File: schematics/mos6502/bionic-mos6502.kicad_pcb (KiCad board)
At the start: 2 copper layers, 48.3 x 71.1 mm, 10 parts, among them J1 Bionic-P135, J2 Bionic-P245, U1 W65C816S, U2 74HC126, U3 11AA010-I/TO

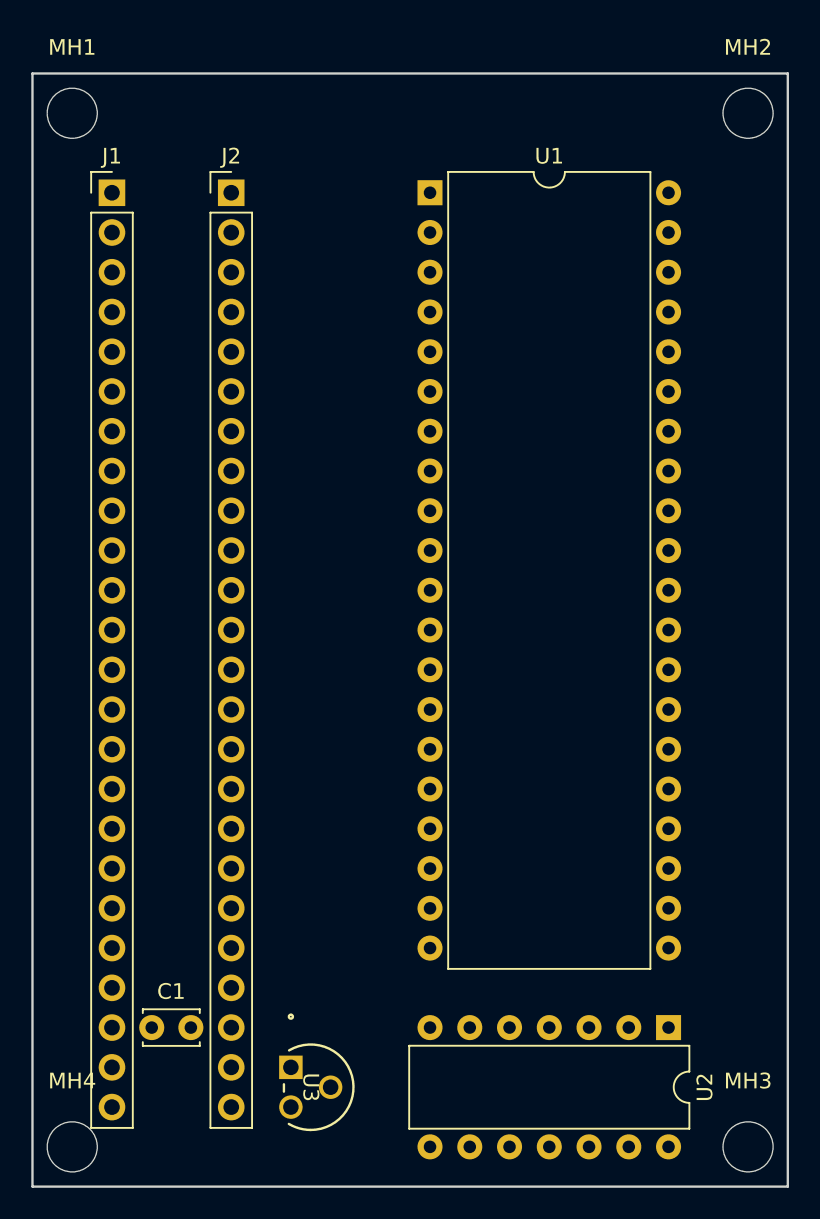
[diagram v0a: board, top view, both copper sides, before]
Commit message: [MOS6502] Remove HC126
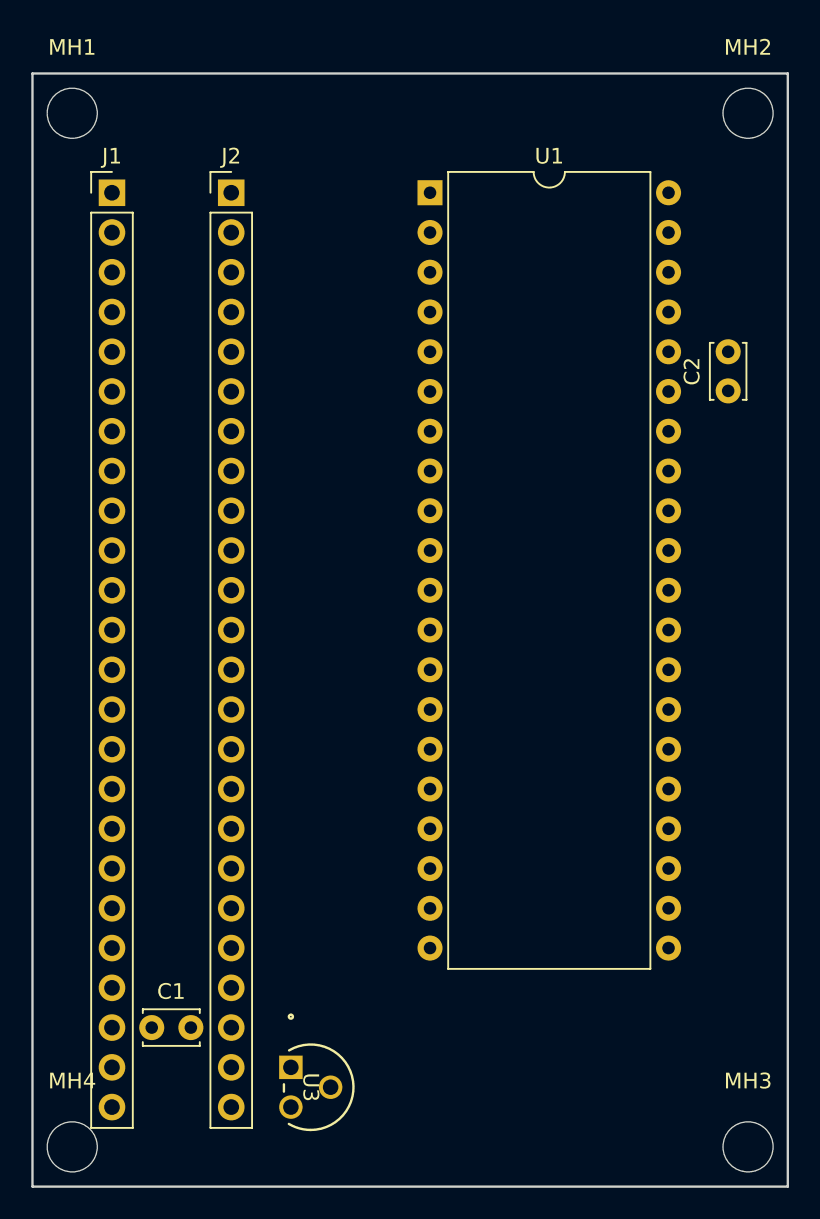
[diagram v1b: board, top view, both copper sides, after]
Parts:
- removed U2: 74HC126, Package_DIP:DIP-14_W7.62mm
- added C2: 0.1u, Capacitor_THT:C_Disc_D3.4mm_W2.1mm_P2.50mm, F.Cu at (142.9, 87.7)
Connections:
- U1 pad 36: Net-(U1-BE) -> /P54
- U1 pad 37: Net-(U1-PHI2I) -> /P46
- U1 pad 40: Net-(U1-~{RES}) -> /P53
